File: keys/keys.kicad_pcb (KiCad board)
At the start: 2 copper layers, 3.3 x 2.9 mm, 69 parts, among them J1 Conn_01x10, J2 Conn_01x02, J3 Conn_01x05, SW1 SW_SPST, SW10 SW_SPST, SW11 SW_SPST, SW12 SW_SPST, SW13 SW_SPST, SW14 SW_SPST, SW15 SW_SPST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

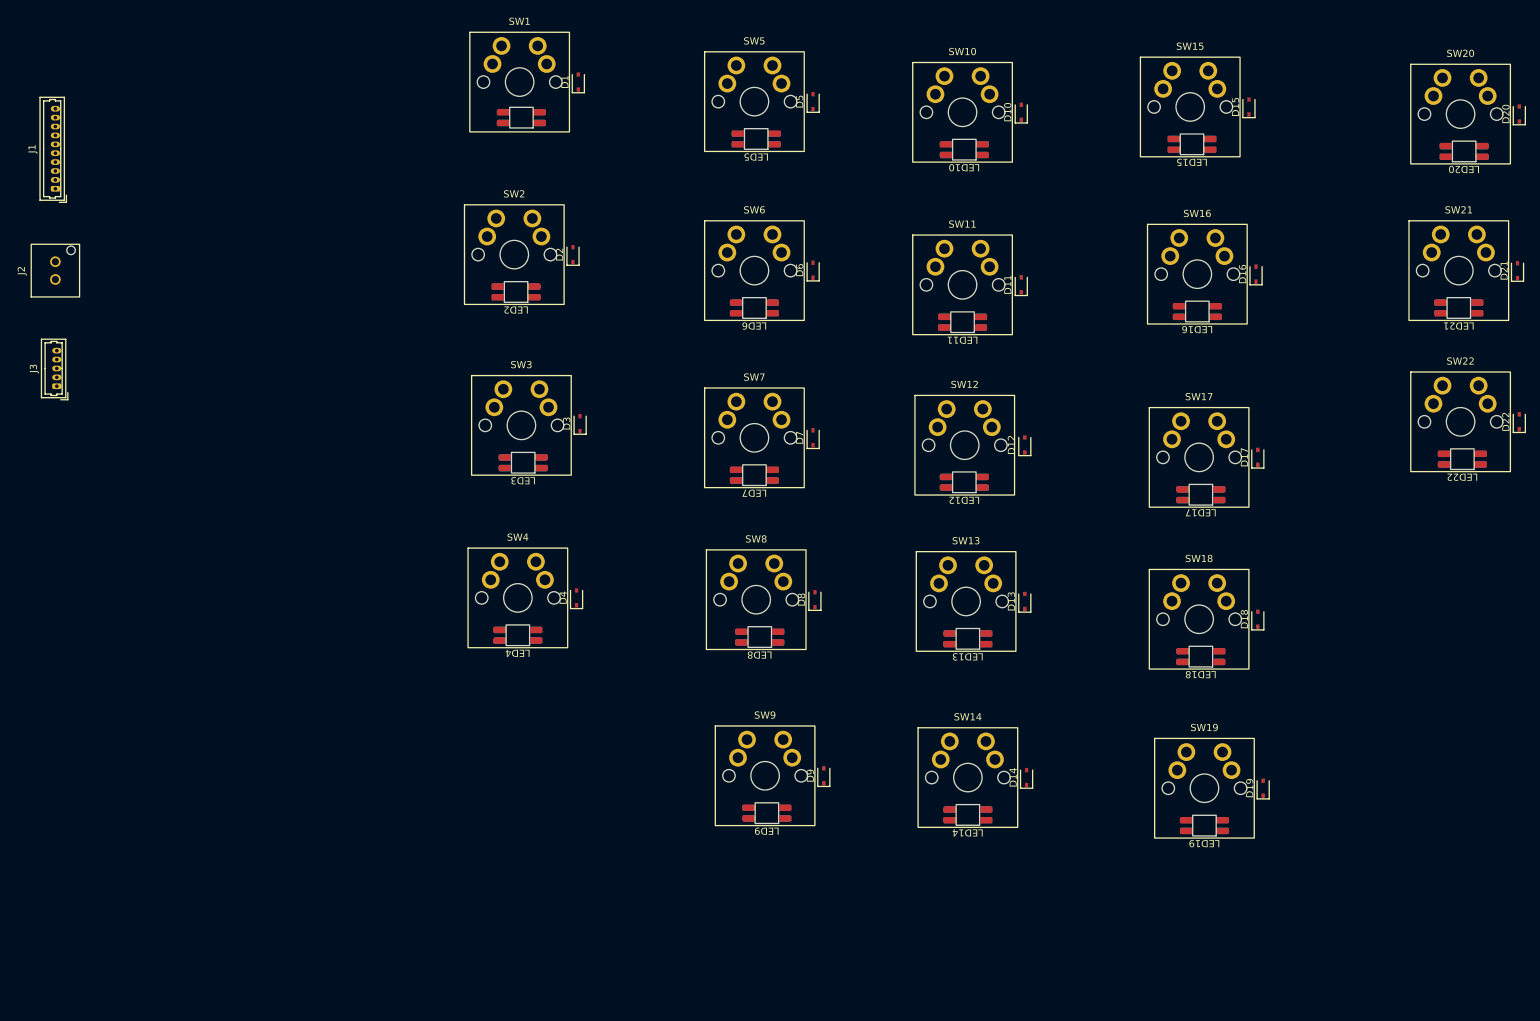
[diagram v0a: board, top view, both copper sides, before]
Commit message: move thumbstick/ to stick/, update keys layout, delete obsolete trackball project
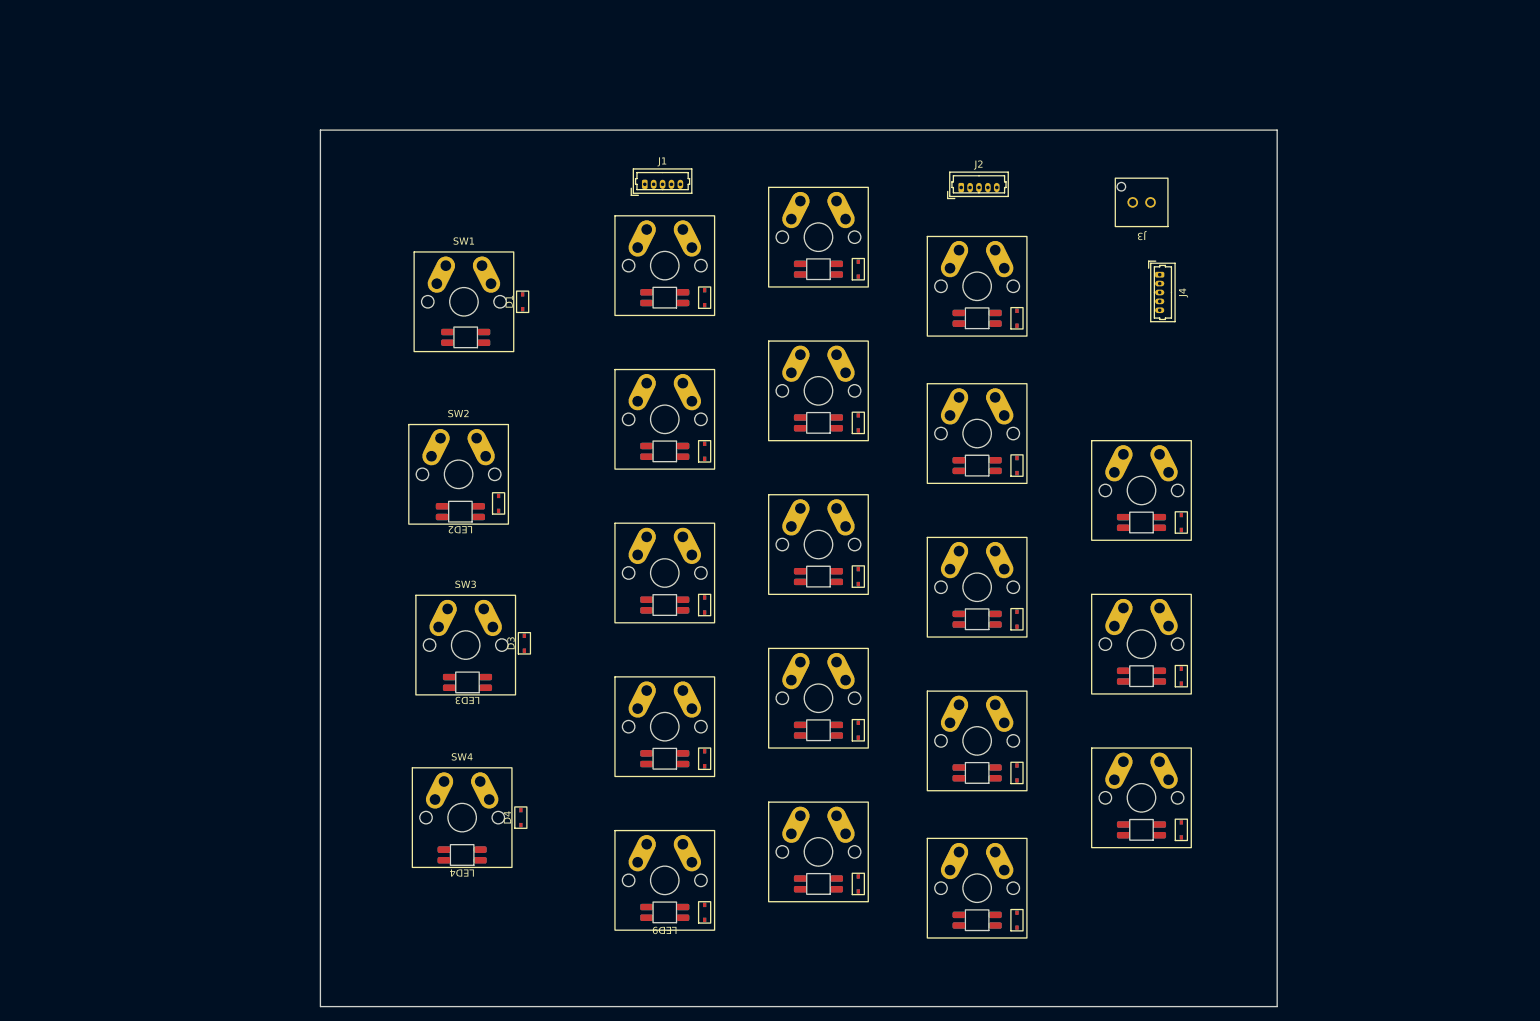
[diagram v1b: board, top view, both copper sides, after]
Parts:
- added J2: Conn_01x05, Connector_Molex:Molex_PicoBlade_53047-0510_1x05_P1.25mm_Vertical, F.Cu at (160.1, 39.8)
- D1, D10, D11, D12, D13, D14, D15, D16, D17, D18, D19, D2, D20, D21, D22, D3, D4, D5, D6, D7, D8, D9: footprint Diode_SMD:D_SOD-323 -> klib:SMD_D-SOD-323-Reversible
- J1: value Conn_01x10 -> Conn_01x05; footprint Connector_Molex:Molex_PicoBlade_53047-1010_1x10_P1.25mm_Vertical -> Connector_Molex:Molex_PicoBlade_53047-0510_1x05_P1.25mm_Vertical
- moved J4 155.8 mm to (188.0, 52.1), turned to -90 degrees
- moved J3 153.0 mm to (185.4, 41.9), turned to 180 degrees
- moved J1 82.8 mm to (115.6, 39.4), turned to 0 degrees
- moved D20 74.5 mm to (191.0, 86.9)
- moved D22 74.5 mm to (191.0, 130.1)
- moved D21 74.0 mm to (191.0, 108.5)
- moved SW20 69.4 mm to (185.4, 82.4)
- moved SW22 69.3 mm to (185.4, 125.6)
- moved LED20 69.1 mm to (185.4, 86.9)
- moved LED22 68.9 mm to (185.4, 130.1)
- moved SW21 68.9 mm to (185.4, 104.0)
- moved LED21 68.3 mm to (185.4, 108.5)
- moved D15 44.1 mm to (167.9, 58.2)
- moved D16 43.0 mm to (167.9, 78.9)
- moved D17 40.8 mm to (167.9, 100.5)
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- renumbered J2 to J3, J3 to J4, LED12 to LEDe
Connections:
- D10 pad 1: COL2 -> COL3
- D11 pad 1: COL2 -> COL3
- D12 pad 1: COL2 -> COL3
- D13 pad 1: COL2 -> COL3
- D14 pad 1: COL2 -> COL3
- D15 pad 1: COL3 -> COL4
- D16 pad 1: COL3 -> COL4
- D17 pad 1: COL3 -> COL4
- D18 pad 1: COL3 -> COL4
- D19 pad 1: COL3 -> COL4
- D20 pad 1: COL4 -> COL5
- D21 pad 1: COL4 -> COL5
- D22 pad 1: COL4 -> COL5
- D5 pad 1: COL1 -> COL2
- D6 pad 1: COL1 -> COL2
- D7 pad 1: COL1 -> COL2
- D8 pad 1: COL1 -> COL2
- D9 pad 1: COL1 -> COL2
- LED10 pad 2: COL2_DIN -> COL3_DIN
- LED15 pad 2: COL3_DIN -> COL4_DIN
- LED20 pad 2: COL4_DIN -> COL5_DIN
- LED5 pad 2: COL1_DIN -> COL2_DIN
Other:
- board size 3.3 x 2.9 mm -> 134.5 x 123.2 mm
